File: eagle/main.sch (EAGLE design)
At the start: 19 parts, among them IC1 74HC164D, IC2 74LS139D, IC3 317EMP, Q1 BSS84, Q2 BSS84, Q3 BSS84, Q4 BSS123, Q5 BSS123

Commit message: Little tweaks.  warning: scribus file is not consistent due to crashiness.
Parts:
- added R1: 3ish, rcl:R-US_R0805
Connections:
- new net N$29: D1.C, R1.2
- net N$14: now also R1.1; no longer D1.C
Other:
- moved on the sheet: D1
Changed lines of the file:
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@@
 <grid distance="0.05" unitdist="inch" unit="inch" style="lines" multiple="1" display="no" altdistance="0.01" altunitdist="inch" altunit="inch"/>
 <layers>
-<layer number="1" name="Top" color="4" fill="1" visible="no" active="no"/>
-<layer number="16" name="Bottom" color="1" fill="1" visible="no" active="no"/>
-<layer number="17" name="Pads" color="2" fill="1" visible="no" active="no"/>
-<layer number="18" name="Vias" color="2" fill="1" visible="no" active="no"/>
-<layer number="19" name="Unrouted" color="6" fill="1" visible="no" active="no"/>
-<layer number="20" name="Dimension" color="15" fill="1" visible="no" active="no"/>
-<layer number="21" name="tPlace" color="7" fill="1" visible="no" active="no"/>
-<layer number="22" name="bPlace" color="7" fill="1" visible="no" active="no"/>
-<layer number="23" name="tOrigins" color="15" fill="1" visible="no" active="no"/>
-<layer number="24" name="bOrigins" color="15" fill="1" visible="no" active="no"/>
-<layer number="25" name="tNames" color="7" fill="1" visible="no" active="no"/>
-<layer number="26" name="bNames" color="7" fill="1" visible="no" active="no"/>
-<layer number="27" name="tValues" color="7" fill="1" visible="no" active="no"/>
-<layer number="28" name="bValues" color="7" fill="1" visible="no" active="no"/>
+<layer number="1" name="Top" color="4" fill="1" visible="yes" active="no"/>
+<layer number="16" name="Bottom" color="1" fill="1" visible="yes" active="no"/>
+<layer number="17" name="Pads" color="2" fill="1" visible="yes" active="no"/>
+<layer number="18" name="Vias" color="2" fill="1" visible="yes" active="no"/>
+<layer number="19" name="Unrouted" color="6" fill="1" visible="yes" active="no"/>
+<layer number="20" name="Dimension" color="15" fill="1" visible="yes" active="no"/>
+<layer number="21" name="tPlace" color="7" fill="1" visible="yes" active="no"/>
+<layer number="22" name="bPlace" color="7" fill="1" visible="yes" active="no"/>
+<layer number="23" name="tOrigins" color="15" fill="1" visible="yes" active="no"/>
+<layer number="24" name="bOrigins" color="15" fill="1" visible="yes" active="no"/>
+<layer number="25" name="tNames" color="7" fill="1" visible="yes" active="no"/>
+<layer number="26" name="bNames" color="7" fill="1" visible="yes" active="no"/>
+<layer number="27" name="tValues" color="7" fill="1" visible="yes" active="no"/>
+<layer number="28" name="bValues" color="7" fill="1" visible="yes" active="no"/>
 <layer number="29" name="tStop" color="7" fill="3" visible="no" active="no"/>
 <layer number="30" name="bStop" color="7" fill="6" visible="no" active="no"/>
@@
 <layer number="35" name="tGlue" color="7" fill="4" visible="no" active="no"/>
 <layer number="36" name="bGlue" color="7" fill="5" visible="no" active="no"/>
-<layer number="37" name="tTest" color="7" fill="1" visible="no" active="no"/>
-<layer number="38" name="bTest" color="7" fill="1" visible="no" active="no"/>
+<layer number="37" name="tTest" color="7" fill="1" visible="yes" active="no"/>
+<layer number="38" name="bTest" color="7" fill="1" visible="yes" active="no"/>
 <layer number="39" name="tKeepout" color="4" fill="11" visible="no" active="no"/>
 <layer number="40" name="bKeepout" color="1" fill="11" visible="no" active="no"/>
@@
 <layer number="44" name="Drills" color="7" fill="1" visible="no" active="no"/>
 <layer number="45" name="Holes" color="7" fill="1" visible="no" active="no"/>
-<layer number="46" name="Milling" color="3" fill="1" visible="no" active="no"/>
-<layer number="47" name="Measures" color="7" fill="1" visible="no" active="no"/>
-<layer number="48" name="Document" color="7" fill="1" visible="no" active="no"/>
-<layer number="49" name="Reference" color="7" fill="1" visible="no" active="no"/>
-<layer number="50" name="dxf" color="7" fill="1" visible="no" active="no"/>
-<layer number="51" name="tDocu" color="7" fill="1" visible="no" active="no"/>
-<layer number="52" name="bDocu" color="7" fill="1" visible="no" active="no"/>
-<layer number="53" name="tGND_GNDA" color="7" fill="9" visible="no" active="no"/>
-<layer number="54" name="bGND_GNDA" color="1" fill="9" visible="no" active="no"/>
-<layer number="56" name="wert" color="7" fill="1" visible="no" active="no"/>
+<layer number="46" name="Milling" color="3" fill="1" visible="yes" active="no"/>
+<layer number="47" name="Measures" color="7" fill="1" visible="yes" active="no"/>
+<layer number="48" name="Document" color="7" fill="1" visible="yes" active="no"/>
+<layer number="49" name="Reference" color="7" fill="1" visible="yes" active="no"/>
+<layer number="50" name="dxf" color="7" fill="1" visible="yes" active="no"/>
+<layer number="51" name="tDocu" color="7" fill="1" visible="yes" active="no"/>
+<layer number="52" name="bDocu" color="7" fill="1" visible="yes" active="no"/>
+<layer number="53" name="tGND_GNDA" color="7" fill="9" visible="yes" active="no"/>
+<layer number="54" name="bGND_GNDA" color="1" fill="9" visible="yes" active="no"/>
+<layer number="56" name="wert" color="7" fill="1" visible="yes" active="no"/>
 <layer number="91" name="Nets" color="2" fill="1" visible="yes" active="yes"/>
 <layer number="92" name="Busses" color="1" fill="1" visible="yes" active="yes"/>
@@
 <part name="P+2" library="supply1" deviceset="VCC" device=""/>
 <part name="IC3" library="linear" deviceset="*317" device="EMP"/>
+<part name="R1" library="rcl" deviceset="R-US_" device="R0805" value="3ish"/>
 </parts>
 <sheets>
@@
 <instance part="GND1" gate="1" x="87.63" y="63.5"/>
 <instance part="C1" gate="G$1" x="73.66" y="69.85" rot="R90"/>
-<instance part="D1" gate="1" x="66.04" y="72.39" rot="R270"/>
+<instance part="D1" gate="1" x="66.04" y="95.25" rot="R270"/>
 <instance part="R3" gate="G$1" x="91.44" y="43.18"/>
 <instance part="GND2" gate="1" x="147.32" y="-27.94"/>
@@
 <instance part="P+2" gate="VCC" x="80.01" y="102.87"/>
 <instance part="IC3" gate="A1" x="57.15" y="104.14"/>
+<instance part="R1" gate="G$1" x="66.04" y="81.28" rot="R90"/>
 </instances>
 <busses>
@@
 <wire x1="71.12" y1="99.06" x2="80.01" y2="99.06" width="0.1524" layer="91"/>
 <pinref part="D1" gate="1" pin="A"/>
-<wire x1="66.04" y1="83.82" x2="66.04" y2="74.93" width="0.1524" layer="91"/>
-<wire x1="66.04" y1="83.82" x2="71.12" y2="99.06" width="0.1524" layer="91"/>
+<wire x1="66.04" y1="97.79" x2="66.04" y2="99.06" width="0.1524" layer="91"/>
+<wire x1="66.04" y1="99.06" x2="71.12" y2="99.06" width="0.1524" layer="91"/>
 <junction x="71.12" y="99.06"/>
 </segment>
@@
 <wire x1="78.74" y1="50.8" x2="74.93" y2="50.8" width="0.1524" layer="91"/>
 <pinref part="430" gate="A" pin="1"/>
-<pinref part="D1" gate="1" pin="C"/>
 <wire x1="71.12" y1="58.42" x2="66.04" y2="58.42" width="0.1524" layer="91"/>
 <wire x1="66.04" y1="58.42" x2="66.04" y2="64.77" width="0.1524" layer="91"/>
 <pinref part="C1" gate="G$1" pin="+"/>
 <wire x1="66.04" y1="64.77" x2="66.04" y2="69.85" width="0.1524" layer="91"/>
-<wire x1="66.04" y1="69.85" x2="71.12" y2="69.85" width="0.1524" layer="91"/>
-<junction x="66.04" y="69.85"/>
+<wire x1="66.04" y1="69.85" x2="66.04" y2="76.2" width="0.1524" layer="91"/>
 <wire x1="66.04" y1="64.77" x2="74.93" y2="64.77" width="0.1524" layer="91"/>
 <junction x="66.04" y="64.77"/>
+<wire x1="71.12" y1="69.85" x2="66.04" y2="69.85" width="0.1524" layer="91"/>
+<junction x="66.04" y="69.85"/>
+<pinref part="R1" gate="G$1" pin="1"/>
 </segment>
 </net>
@@
 </segment>
 </net>
+<net name="N$29" class="0">
+<segment>
+<pinref part="D1" gate="1" pin="C"/>
+<wire x1="66.04" y1="86.36" x2="66.04" y2="92.71" width="0.1524" layer="91"/>
+<pinref part="R1" gate="G$1" pin="2"/>
+</segment>
+</net>

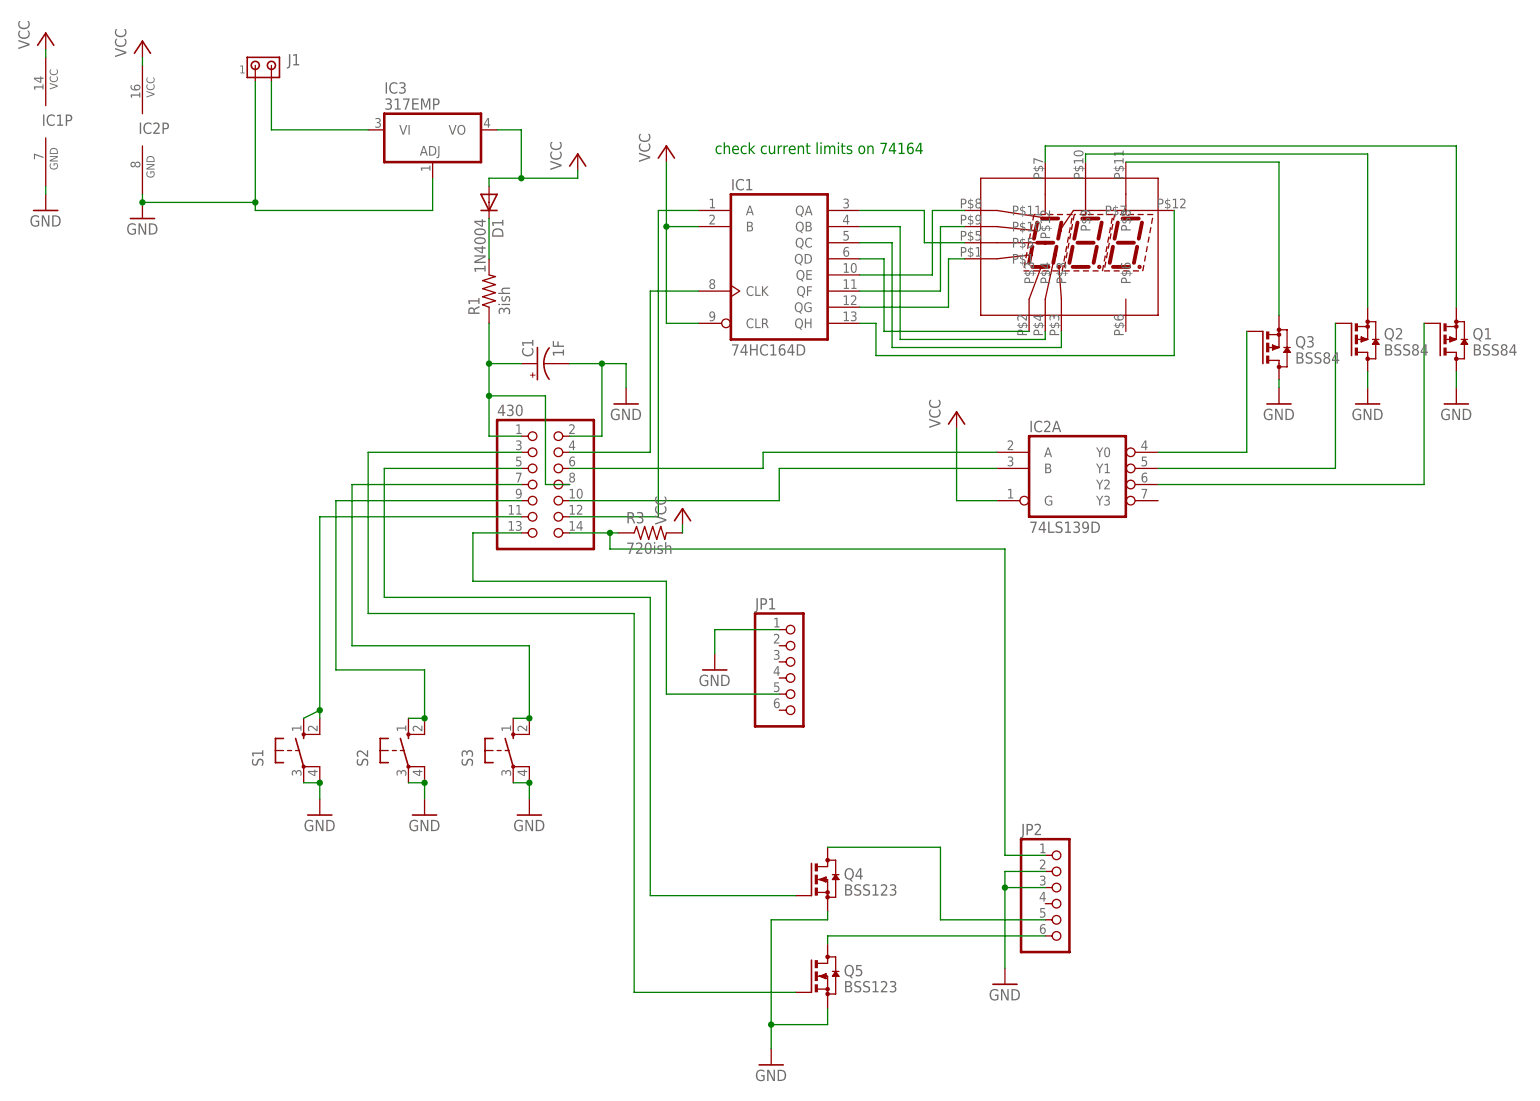
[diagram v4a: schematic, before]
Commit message: Fixed up the layout a little, made the mask files consistent
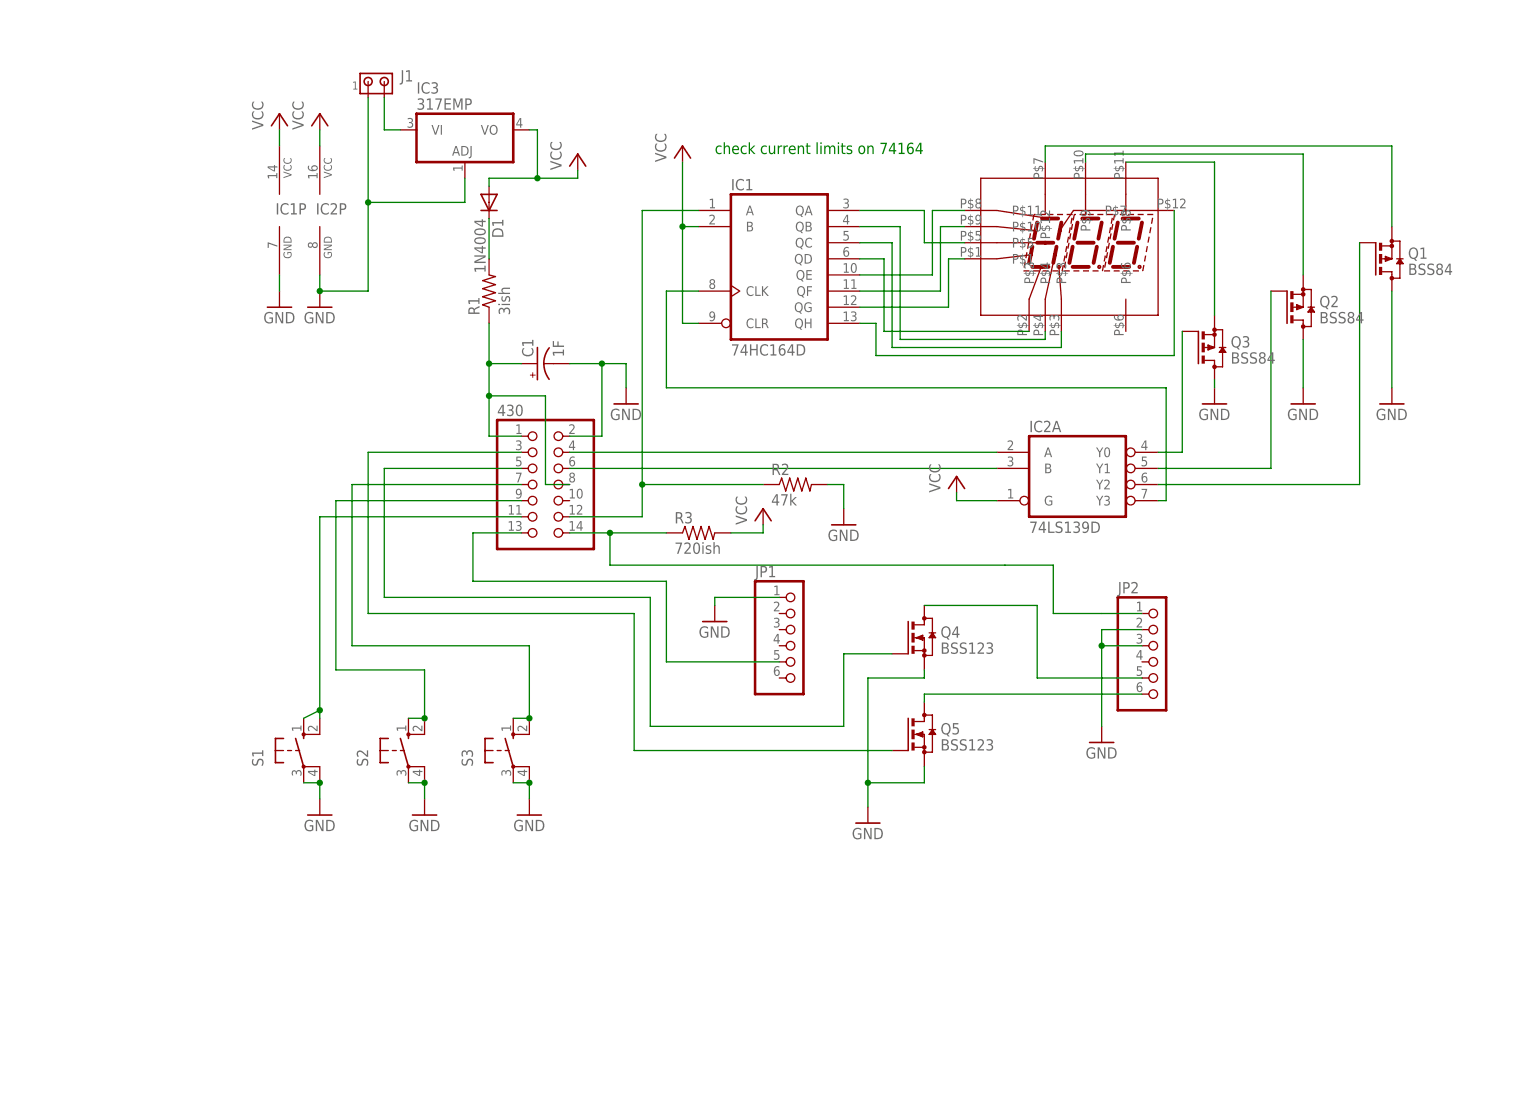
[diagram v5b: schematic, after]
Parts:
- added R2: 47k, rcl:R-US_R0805
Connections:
- net GND: now also R2.2
- net N$12: now also R2.1
- net N$13: now also IC2A.Y3; no longer 430.4
- net N$21: now also 430.6; no longer 430.10
- net N$22: now also 430.4; no longer 430.6
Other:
- moved on the sheet: IC1P, IC2P, IC3, J1, JP1, JP2, Q1, Q2, Q3, Q4, Q5, R3

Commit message: snapshot before porting code to v4 hardware
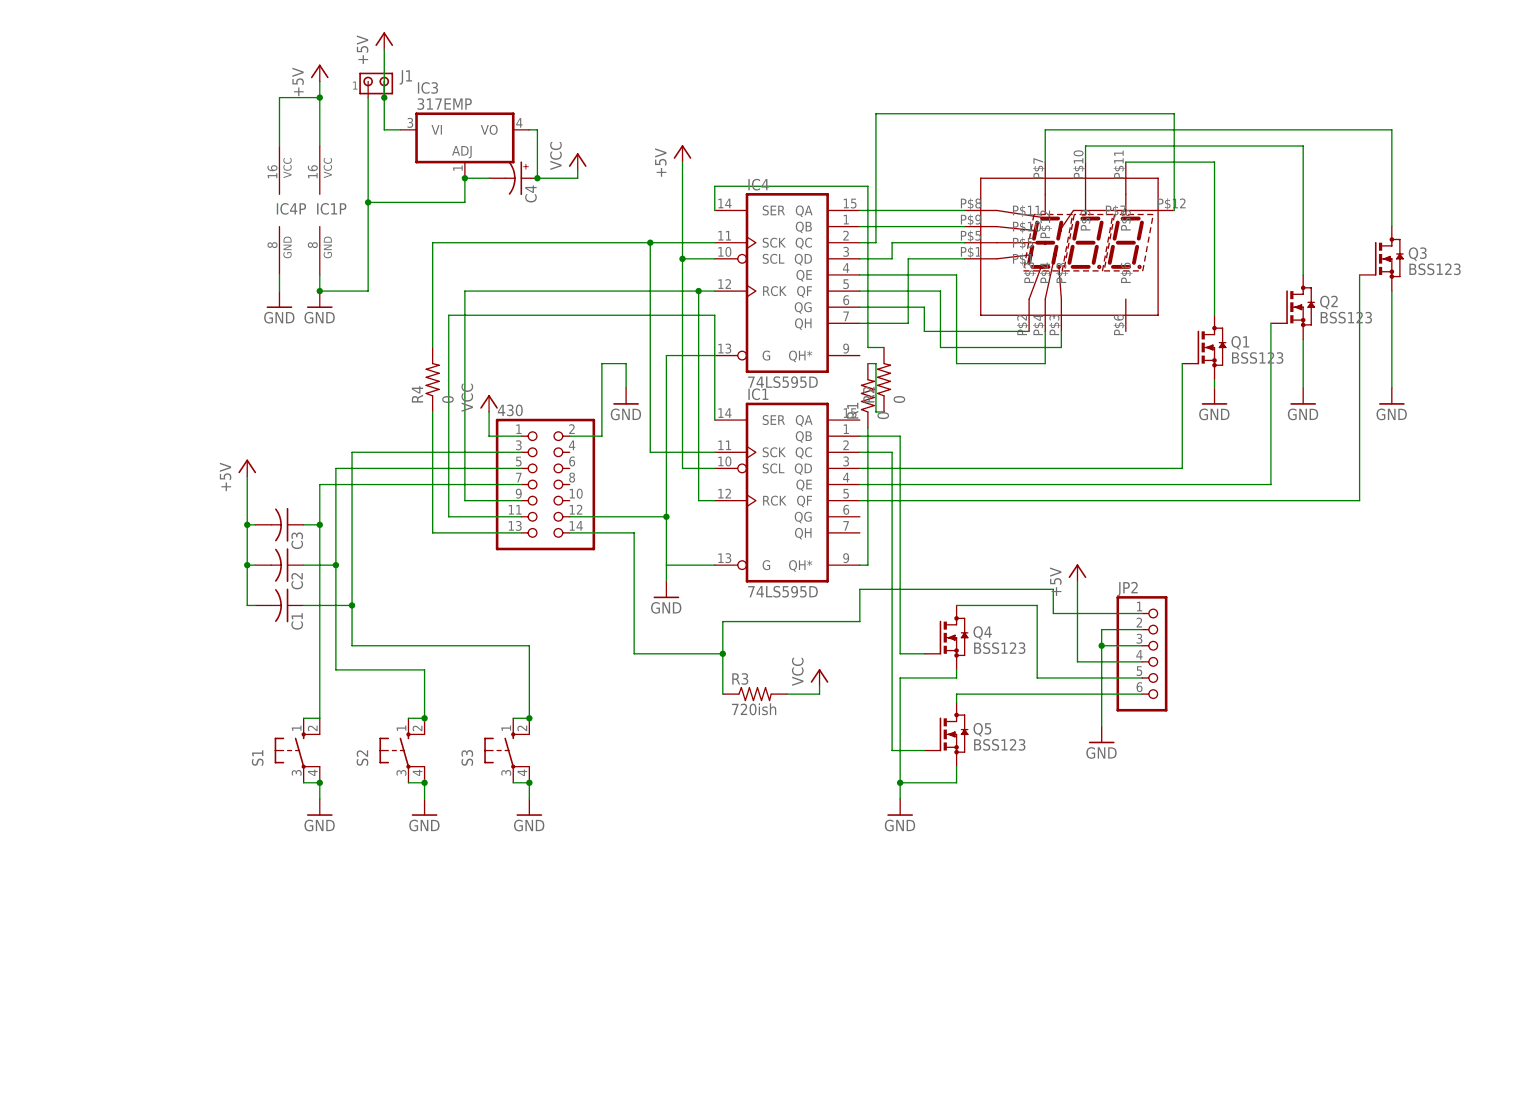
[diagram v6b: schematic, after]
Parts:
- removed D1: 1N4004, diode:1N4004
- removed IC2: 74LS139D, 74xx-us:74LS139D
- removed JP1: (no value), pinhead:PINHD-1X6/90
- added C2, C3: (no value), rcl:C-USC0603K
- added C4: (no value), rcl:CPOL-USE5-8.5
- added IC4: 74LS595D, 74xx-us:74LS595D
- added R4: 0, rcl:R-US_R0603
- C1: value 1F -> (none); device rcl:CPOL-USE5-13 -> rcl:C-USC0603K
- IC1: value 74HC164D -> 74LS595D; device 74xx-us:74HC164D -> 74xx-us:74LS595D
- Q1, Q2, Q3: value BSS84 -> BSS123; device transistor-small-signal:BSS84 -> transistor-small-signal:BSS123
- R1: value 3ish -> 0; device rcl:R-US_R0805 -> rcl:R-US_R0603
- R2: value 47k -> 0; device rcl:R-US_R0805 -> rcl:R-US_R0603
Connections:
- removed net N$30: IC3.VI, J1.2
- new net +5V: C1.2, C2.2, C3.2, IC1A.SCL, IC1P.VCC, IC3.VI, IC4A.SCL, IC4P.VCC, J1.2, JP2.4
- net GND: now also 430.12, C4.-, IC1A.G, IC4A.G, IC4P.GND, Q1.S, Q2.S, Q3.S; no longer C1.-, IC2P.GND, JP1.1, Q1.D, Q2.D, Q3.D, R2.2
- net N$1: now also IC4A.QA, U$1.P$11; no longer IC1A.QF, U$1.P$10
- net N$10: now also Q2.D; no longer Q2.S
- net N$11: now also Q3.D; no longer Q1.S
- net N$12: now also IC1A.QD, Q1.G; no longer 430.12, IC1A.A, R2.1
- net N$13: now also 430.11, IC1A.SER; no longer IC1A.CLK, IC2A.Y3
- net N$14: now also IC4A.SER, R2.2; no longer 430.1, 430.8, C1.+, R1.1
- net N$15: now also 430.7, C3.1; no longer 430.11
- net N$16: now also IC1A.QH*, R1.1; no longer 430.9, S2.S, S2.S1
- net N$18: now also 430.3, C1.1; no longer 430.7
- net N$19: now also R1.2, R2.1; no longer 430.3, Q5.G
- net N$2: now also IC4A.QB, U$1.P$10; no longer IC1A.QE, U$1.P$11
- net N$20: now also IC1A.QB; no longer 430.5
- net N$21: now also IC1A.SCK, IC4A.SCK, R4.2; no longer 430.6, IC2A.B
- net N$22: now also IC1A.QE, Q2.G; no longer 430.4, IC2A.A
- net N$24: now also IC1A.QF, Q3.G; no longer 430.13, JP1.5
- net N$25: now also IC1A.QC, Q5.G; no longer IC2A.Y0, Q3.G
- net N$26: now also 430.13, R4.1; no longer IC2A.Y1, Q2.G
- net N$27: now also 430.9, IC1A.RCK, IC4A.RCK; no longer IC2A.Y2, Q1.G
- net N$29: now also 430.5, C2.1, S2.S, S2.S1; no longer D1.C, R1.2
- net N$3: now also IC4A.QH, U$1.P$1; no longer IC1A.QA, U$1.P$5
- net N$4: now also IC4A.QG, U$1.P$2; no longer IC1A.QG, U$1.P$1
- net N$5: now also IC4A.QF, U$1.P$3; no longer IC1A.QD, U$1.P$2
- net N$6: now also IC4A.QE; no longer IC1A.QB
- net N$7: now also IC4A.QD, U$1.P$5; no longer IC1A.QC, U$1.P$3
- net N$8: now also IC4A.QC; no longer IC1A.QH
- net N$9: now also Q1.D; no longer Q3.S
- net VCC: now also 430.1, C4.+; no longer D1.A, IC1A.B, IC1A.CLR, IC1P.VCC, IC2A.G, IC2P.VCC
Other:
- note removed: "check current limits on 74164"
- moved on the sheet: IC1P, Q4, Q5, R1, R2, R3

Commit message: another big revamp
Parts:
- added J2: (no value), con-amp:MTA02-100
- C4: device rcl:CPOL-USE5-8.5 -> rcl:CPOL-USE2.5-7
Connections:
- removed net N$27: 430.9, IC1A.RCK, IC4A.RCK
- new net N$30: 430.6, IC1A.RCK, IC4A.RCK
- new net N$31: 430.9, R3.2
- net +5V: no longer C1.2, C2.2, C3.2, IC1A.SCL, IC1P.VCC, IC4A.SCL, IC4P.VCC
- net GND: now also 430.13, J2.2; no longer 430.12
- net N$13: now also 430.14; no longer 430.11
- net N$17: now also 430.11, J2.1; no longer 430.14
- net N$26: now also 430.12; no longer 430.13
- net VCC: now also C1.2, C2.2, C3.2, IC1A.SCL, IC1P.VCC, IC4A.SCL, IC4P.VCC; no longer R3.2
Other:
- moved on the sheet: R3
